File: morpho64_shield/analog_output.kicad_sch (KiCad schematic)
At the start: 13 parts, among them J5 Conn_Coaxial_Small, Q1 FMMT493TC, Q2 FMMT593TC, U5 OPA596DBVR, U6 OPA596DBVR

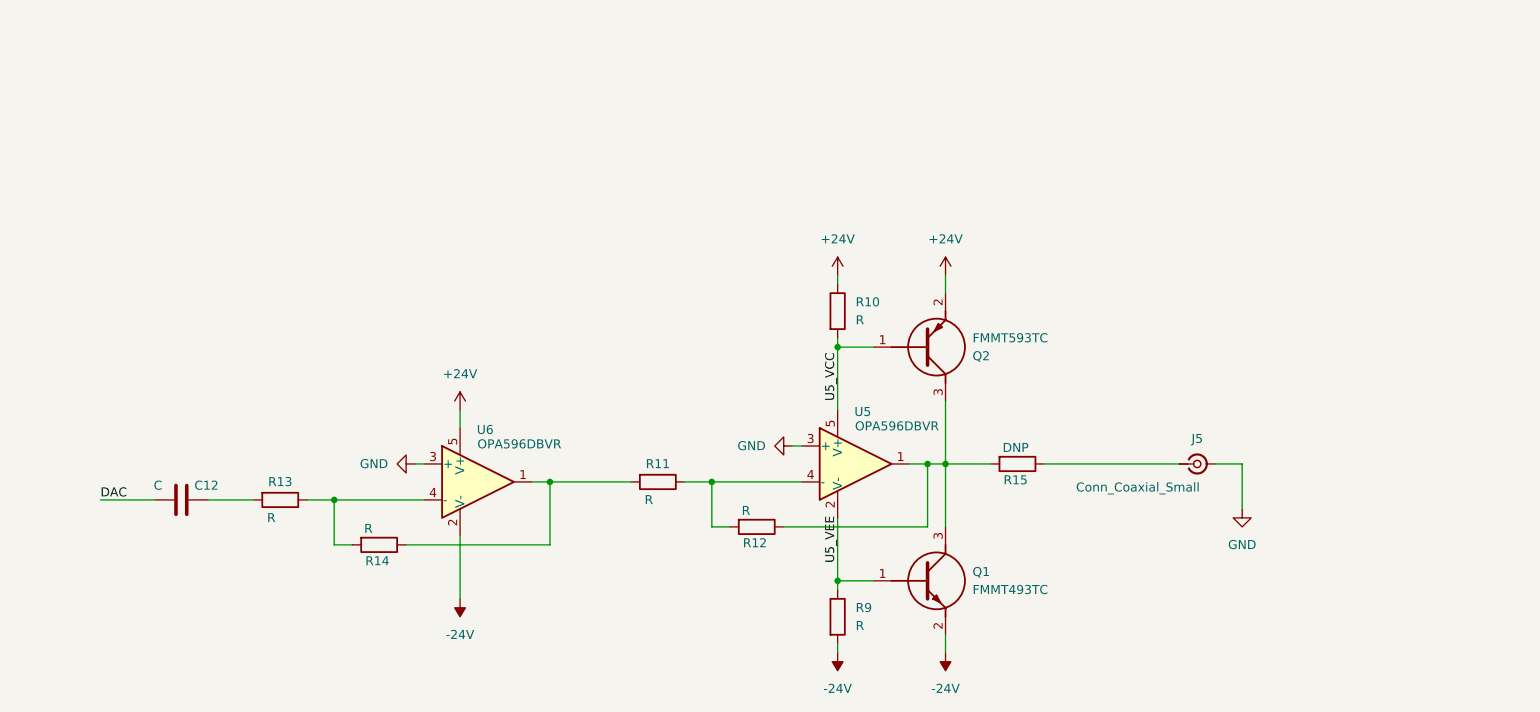
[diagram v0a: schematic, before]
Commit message: esd + caps
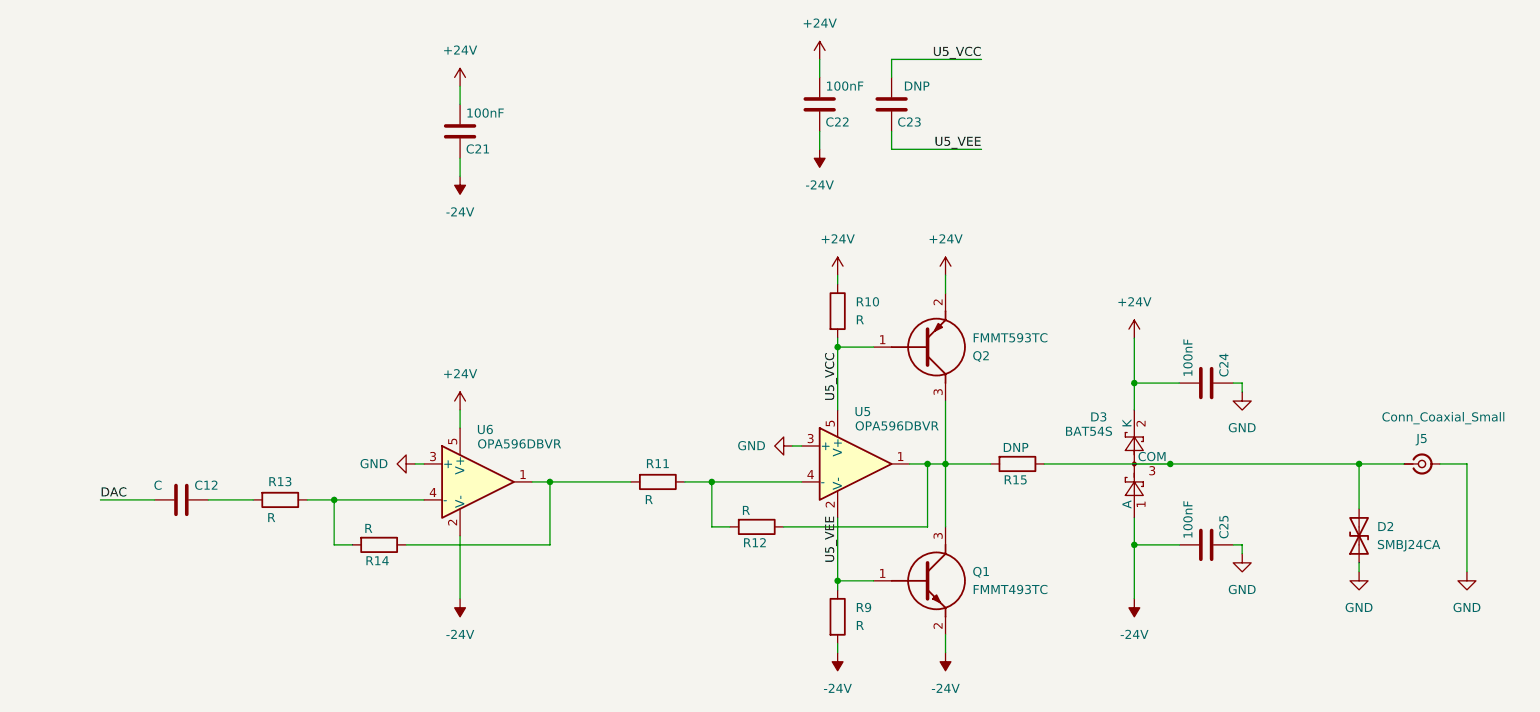
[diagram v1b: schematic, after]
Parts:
- added C21, C22, C24, C25: 100nF, symbol Device:C
- added C23: DNP, symbol Device:C
- added D2: SMBJ24CA, symbol Device:D_TVS
- added D3: BAT54S, Package_TO_SOT_SMD:SOT-23, symbol Diode:BAT54S
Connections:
- net +24V: now also C21.2, C22.2, C24.2, D3.2 (K)
- net -24V: now also C21.1, C22.1, C25.2, D3.1 (A)
- net GND: now also C24.1, C25.1, D2.1 (A1)
- net U5_VCC: now also C23.2
- net U5_VEE: now also C23.1
- net at J5.1 (In), R15.1: now also D2.2 (A2), D3.3 (COM)
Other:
- moved on the sheet: J5

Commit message: First part of layout
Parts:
- C12, C21, C22, C23, C24, C25: footprint (none) -> Capacitor_SMD:C_0603_1608Metric
- D2: footprint (none) -> Diode_SMD:D_SMB
- R10, R11, R12, R13, R14, R15, R9: footprint (none) -> Resistor_SMD:R_0603_1608Metric
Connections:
- net at D2.2 (A2), J5.1 (In), R15.1: no longer D3.3 (COM)
- net DAC renamed DAC_out
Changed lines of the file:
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@@
 	)
 	(junction
-		(at 185.42 82.55)
-		(diameter 0)
-		(color 0 0 0 0)
-	)
-	(junction
 		(at 180.34 71.12)
 		(diameter 0)
@@
 	(wire
 		(pts
-			(xy 185.42 82.55) (xy 212.09 82.55)
-		)
-		(stroke
-			(width 0)
-			(type default)
-		)
-	)
-	(wire
-		(pts
 			(xy 212.09 82.55) (xy 218.44 82.55)
 		)
@@
 	(wire
 		(pts
-			(xy 167.64 82.55) (xy 185.42 82.55)
+			(xy 167.64 82.55) (xy 212.09 82.55)
 		)
 		(stroke
@@
 		)
 	)
+	(global_label "DAC_out"
+		(shape input)
+		(at 34.29 87.63 180)
+		(fields_autoplaced yes)
+		(effects
+			(font
+				(size 1.27 1.27)
+			)
+			(justify right)
+		)
+		(property "Intersheetrefs" "${INTERSHEET_REFS}"
+			(at 23.6849 87.63 0)
+			(hide yes)
+			(show_name no)
+			(do_not_autoplace no)
+			(effects
+				(font
+					(size 1.27 1.27)
+				)
+				(justify right)
+			)
+		)
+	)
 	(symbol
 		(lib_id "power:GND")
@@
 			)
 		)
-		(property "Footprint" ""
+		(property "Footprint" "Resistor_SMD:R_0603_1608Metric"
 			(at 127 89.662 90)
 			(hide yes)
@@
 			)
 		)
-		(property "Footprint" ""
+		(property "Footprint" "Resistor_SMD:R_0603_1608Metric"
 			(at 136.652 60.96 90)
 			(hide yes)
@@
 			)
 		)
-		(property "Footprint" ""
+		(property "Footprint" "Capacitor_SMD:C_0603_1608Metric"
 			(at 134.9248 27.94 0)
 			(hide yes)
@@
 			)
 		)
-		(property "Footprint" ""
+		(property "Footprint" "Capacitor_SMD:C_0603_1608Metric"
 			(at 84.1248 31.75 0)
 			(hide yes)
@@
 			)
 		)
-		(property "Footprint" ""
+		(property "Footprint" "Capacitor_SMD:C_0603_1608Metric"
 			(at 49.53 86.6648 0)
 			(hide yes)
@@
 			)
 		)
-		(property "Footprint" ""
+		(property "Footprint" "Capacitor_SMD:C_0603_1608Metric"
 			(at 186.69 72.0852 0)
 			(hide yes)
@@
 			)
 		)
-		(property "Footprint" ""
+		(property "Footprint" "Resistor_SMD:R_0603_1608Metric"
 			(at 73.66 92.202 90)
 			(hide yes)
@@
 			)
 		)
-		(property "Footprint" ""
+		(property "Footprint" "Diode_SMD:D_SMB"
 			(at 212.09 92.71 0)
 			(hide yes)
@@
 			)
 		)
-		(property "Footprint" ""
+		(property "Footprint" "Resistor_SMD:R_0603_1608Metric"
 			(at 163.83 80.772 90)
 			(hide yes)
@@
 			)
 		)
-		(property "Footprint" ""
+		(property "Footprint" "Resistor_SMD:R_0603_1608Metric"
 			(at 59.69 85.852 90)
 			(hide yes)
@@
 			)
 		)
-		(property "Footprint" ""
+		(property "Footprint" "Resistor_SMD:R_0603_1608Metric"
 			(at 136.652 104.14 90)
 			(hide yes)
@@
 			)
 		)
-		(property "Footprint" ""
+		(property "Footprint" "Capacitor_SMD:C_0603_1608Metric"
 			(at 145.0848 27.94 0)
 			(hide yes)
@@
 			)
 		)
-		(property "Footprint" ""
+		(property "Footprint" "Resistor_SMD:R_0603_1608Metric"
 			(at 113.03 83.312 90)
 			(hide yes)
@@
 			)
 		)
-		(property "Footprint" ""
+		(property "Footprint" "Capacitor_SMD:C_0603_1608Metric"
 			(at 186.69 94.9452 0)
 			(hide yes)

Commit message: First PCB order
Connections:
- net at D3.3 (COM): now also D2.2 (A2), J5.1 (In), R15.1
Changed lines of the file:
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@@
+	)
+	(junction
+		(at 185.42 82.55)
+		(diameter 0)
+		(color 0 0 0 0)
 	)
 	(junction
@@
 	(wire
 		(pts
+			(xy 185.42 82.55) (xy 212.09 82.55)
+		)
+		(stroke
+			(width 0)
+			(type default)
+		)
+	)
+	(wire
+		(pts
 			(xy 49.53 87.63) (xy 55.88 87.63)
 		)
@@
 	(wire
 		(pts
-			(xy 167.64 82.55) (xy 212.09 82.55)
-		)
-		(stroke
+			(xy 167.64 82.55) (xy 185.42 82.55)
+		)
+		(stroke

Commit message: First PCB assebled
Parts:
- C12: value C -> 10u
- R10, R9: value R -> 100R
- R11, R12, R13: value R -> 33k
- R14: value R -> 470k
- R15: value DNP -> 0R
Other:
- note added: "Dioda?"
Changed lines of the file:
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@@
 	(generator_version "10.0")
 	(paper "A4")
+	(text "Dioda? \n"
+		(exclude_from_sim no)
+		(at 40.64 82.296 0)
+		(effects
+			(font
+				(size 1.27 1.27)
+			)
+		)
+	)
 	(junction
 		(at 212.09 82.55)
@@
 			)
 		)
-		(property "Value" "R"
+		(property "Value" "33k"
 			(at 125.476 89.154 90)
 			(show_name no)
@@
 			)
 		)
-		(property "Value" "R"
+		(property "Value" "100R"
 			(at 140.97 62.2299 0)
 			(show_name no)
@@
 			)
 		)
-		(property "Value" "C"
+		(property "Value" "10u"
 			(at 42.418 85.598 90)
 			(show_name no)
@@
 			)
 		)
-		(property "Value" "R"
+		(property "Value" "470k"
 			(at 72.136 91.694 90)
 			(show_name no)
@@
 			)
 		)
-		(property "Value" "DNP"
+		(property "Value" "0R"
 			(at 163.576 80.264 90)
 			(show_name no)
@@
 			)
 		)
-		(property "Value" "R"
+		(property "Value" "33k"
 			(at 58.42 90.17 90)
 			(show_name no)
@@
 			)
 		)
-		(property "Value" "R"
+		(property "Value" "100R"
 			(at 140.97 105.4099 0)
 			(show_name no)
@@
 			)
 		)
-		(property "Value" "R"
+		(property "Value" "33k"
 			(at 111.76 87.63 90)
 			(show_name no)
